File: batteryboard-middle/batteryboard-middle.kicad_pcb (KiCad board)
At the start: 2 copper layers, 46.8 x 46.8 mm, 9 parts, among them J1 FLE-107-01-G-DV-A, J2 Conn_01x02, J3 Conn_01x02, J4 FTS-107-01-L-DV-A

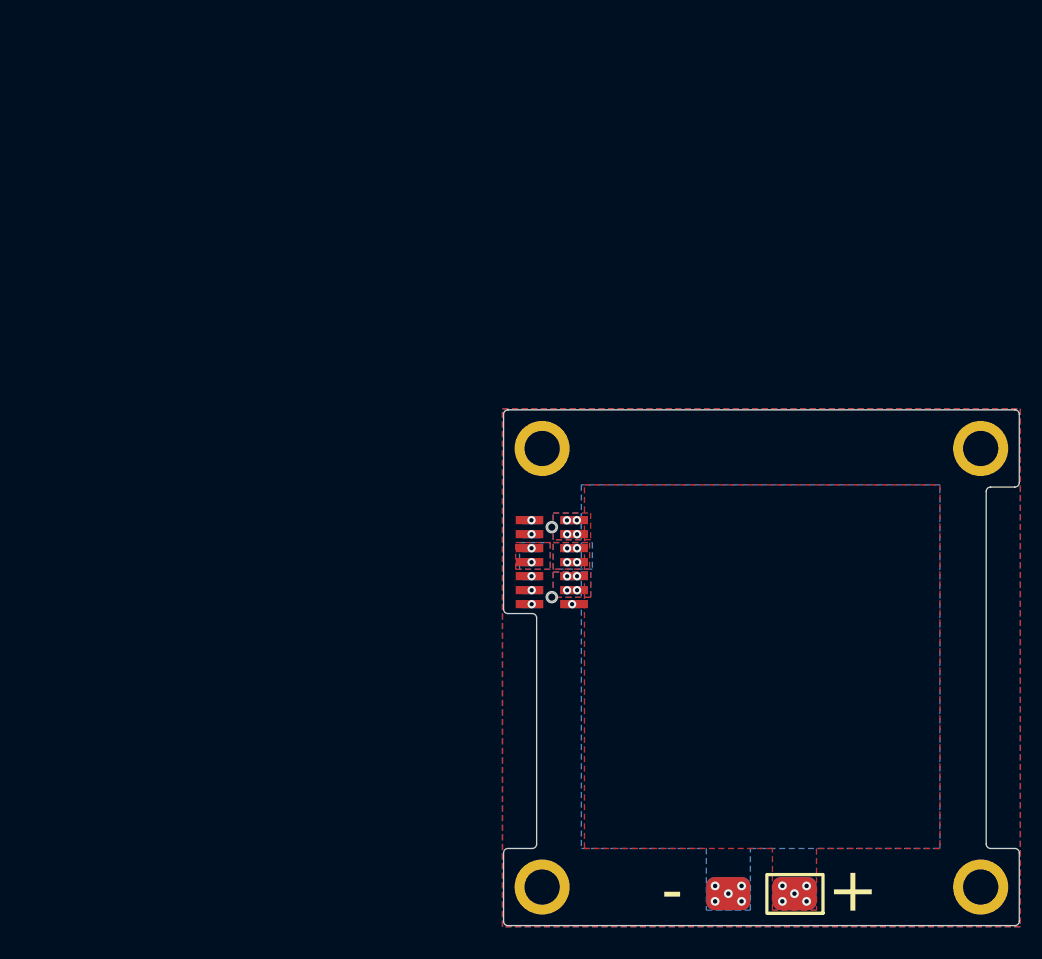
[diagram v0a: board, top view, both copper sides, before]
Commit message: Updated batteryboards for Rev B3/01
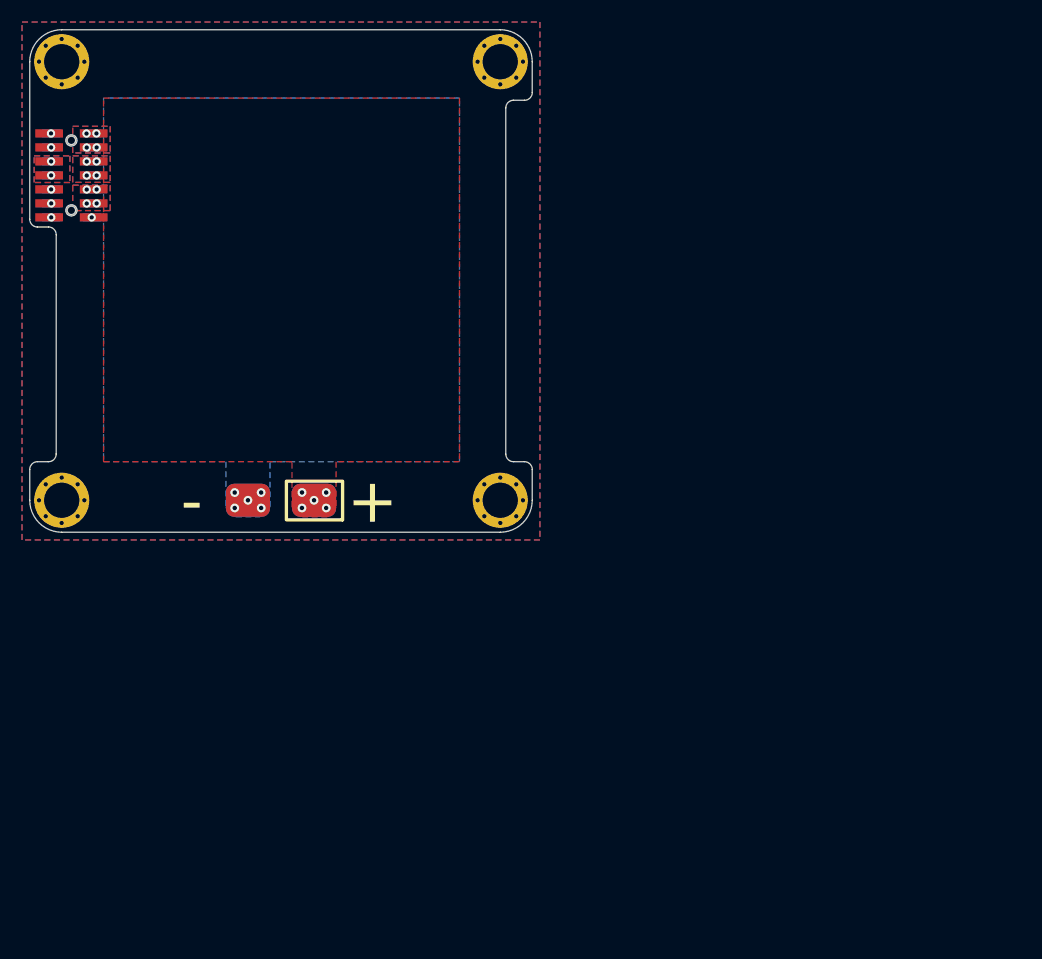
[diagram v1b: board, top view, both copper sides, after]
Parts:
- J1: value FLE-107-01-G-DV-A -> FLE-107-01-X-DV-A; footprint batteryboard:SAMTEC_FLE-107-01-G-DV-A -> batteryboard:SAMTEC_FLE-107-01-X-DV-A
- J2: renamed from J4; value FTS-107-01-L-DV-A -> FTS-107-01-X-DV-A
- J3: value Conn_01x02 -> Battery Pads
- J4: renamed from J2; value Conn_01x02 -> Battery Pads
- moved J3 56.4 mm to (103.2, 85.4)
- moved J4 56.4 mm to (103.2, 85.4)
- moved Ref** 56.2 mm to (103.0, 45.0)
- moved H4 56.0 mm to (83.3, 45.6)
- moved H1 56.0 mm to (123.1, 45.6)
- moved H3 56.0 mm to (83.3, 85.4)
- moved J1 56.0 mm to (84.2, 55.9)
- moved J2 56.0 mm to (84.2, 55.9)
- moved H2 56.0 mm to (123.1, 85.4)
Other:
- board size 46.8 x 46.8 mm -> 45.6 x 45.6 mm
- board text added: "18-FEB-23"
- board text added: "Rev B3/01"
- board text removed: "06-NOV-22"
- board text removed: "Rev B2/01"

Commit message: Exported Gerbers
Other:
- rule pad_to_mask_clearance: 0 -> 0.0508

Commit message: Rev B3/02 updates
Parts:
- added REF**: Fiducial_1mm_Mask2mm, Fiducial:Fiducial_1mm_Mask2mm, F.Cu at (119.1, 85.4)
- added REF**: Fiducial_1mm_Mask2mm, Fiducial:Fiducial_1mm_Mask2mm, F.Cu at (119.1, 45.6)
- added REF**: Fiducial_1mm_Mask2mm, Fiducial:Fiducial_1mm_Mask2mm, F.Cu at (87.3, 45.6)
- added REF**: Fiducial_1mm_Mask2mm, Fiducial:Fiducial_1mm_Mask2mm, B.Cu at (87.3, 45.6)
- added REF**: Fiducial_1mm_Mask2mm, Fiducial:Fiducial_1mm_Mask2mm, B.Cu at (119.1, 85.4)
- added REF**: Fiducial_1mm_Mask2mm, Fiducial:Fiducial_1mm_Mask2mm, B.Cu at (119.1, 45.6)
- moved Ref** 0.90 mm to (103.9, 45.0)
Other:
- board text added: "12-APR-23"
- board text added: "Rev B3/02"
- board text removed: "18-FEB-23"
- board text removed: "Rev B3/01"
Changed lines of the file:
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@@
     )
+  )
+  (footprint "Fiducial:Fiducial_1mm_Mask2mm" (layer "F.Cu")
+    (at 119.1 85.4)
+    (descr "Circular Fiducial, 1mm bare copper, 2mm soldermask opening (Level A)")
+    (tags "fiducial")
+    (attr smd)
+    (fp_text reference "REF**" (at 0 -2) (layer "F.SilkS") hide
+        (effects (font (size 1 1) (thickness 0.15)))
+    )
+    (fp_text value "Fiducial_1mm_Mask2mm" (at 0 2) (layer "F.Fab")
+        (effects (font (size 1 1) (thickness 0.15)))
+    )
+    (fp_circle (center 0 0) (end 1.25 0)
+      (stroke (width 0.05) (type solid)) (fill none) (layer "F.CrtYd"))
+    (pad "" smd circle (at 0 0) (size 1 1) (layers "F.Cu" "F.Mask")
+      (solder_mask_margin 0.5) (clearance 0.5))
   )
   (footprint "custom-footprints:pycubed_mini_half" (layer "F.Cu")
-    (at 103 45)
+    (at 103.9 45)
     (attr through_hole)
     (fp_text reference "Ref**" (at 0 0) (layer "F.SilkS") hide
@@
       (net 3 "GND") (pinfunction "1") (pintype "input"))
   )
+  (footprint "Fiducial:Fiducial_1mm_Mask2mm" (layer "F.Cu")
+    (at 119.1 45.6)
+    (descr "Circular Fiducial, 1mm bare copper, 2mm soldermask opening (Level A)")
+    (tags "fiducial")
+    (attr smd)
+    (fp_text reference "REF**" (at 0 -2) (layer "F.SilkS") hide
+        (effects (font (size 1 1) (thickness 0.15)))
+    )
+    (fp_text value "Fiducial_1mm_Mask2mm" (at 0 2) (layer "F.Fab")
+        (effects (font (size 1 1) (thickness 0.15)))
+    )
+    (fp_circle (center 0 0) (end 1.25 0)
+      (stroke (width 0.05) (type solid)) (fill none) (layer "F.CrtYd"))
+    (pad "" smd circle (at 0 0) (size 1 1) (layers "F.Cu" "F.Mask")
+      (solder_mask_margin 0.5) (clearance 0.5))
+  )
+  (footprint "Fiducial:Fiducial_1mm_Mask2mm" (layer "F.Cu")
+    (at 87.3 45.6)
+    (descr "Circular Fiducial, 1mm bare copper, 2mm soldermask opening (Level A)")
+    (tags "fiducial")
+    (attr smd)
+    (fp_text reference "REF**" (at 0 -2) (layer "F.SilkS") hide
+        (effects (font (size 1 1) (thickness 0.15)))
+    )
+    (fp_text value "Fiducial_1mm_Mask2mm" (at 0 2) (layer "F.Fab")
+        (effects (font (size 1 1) (thickness 0.15)))
+    )
+    (fp_circle (center 0 0) (end 1.25 0)
+      (stroke (width 0.05) (type solid)) (fill none) (layer "F.CrtYd"))
+    (pad "" smd circle (at 0 0) (size 1 1) (layers "F.Cu" "F.Mask")
+      (solder_mask_margin 0.5) (clearance 0.5))
+  )
   (footprint "batteryboard:Battery Pads" (layer "B.Cu")
     (at 103.2 85.4 180)
@@
     (pad "2" smd roundrect (at 3 0 180) (size 4 3) (layers "B.Cu" "B.Paste" "B.Mask") (roundrect_rratio 0.25)
       (net 2 "BATT_N_SW") (pinfunction "Pin_2") (pintype "passive"))
+  )
+  (footprint "Fiducial:Fiducial_1mm_Mask2mm" (layer "B.Cu")
+    (at 87.3 45.6 180)
+    (descr "Circular Fiducial, 1mm bare copper, 2mm soldermask opening (Level A)")
+    (tags "fiducial")
+    (attr smd)
+    (fp_text reference "REF**" (at 0 2) (layer "B.SilkS") hide
+        (effects (font (size 1 1) (thickness 0.15)) (justify mirror))
+    )
+    (fp_text value "Fiducial_1mm_Mask2mm" (at 0 -2) (layer "B.Fab")
+        (effects (font (size 1 1) (thickness 0.15)) (justify mirror))
+    )
+    (fp_circle (center 0 0) (end 1.25 0)
+      (stroke (width 0.05) (type solid)) (fill none) (layer "B.CrtYd"))
+    (pad "" smd circle (at 0 0 180) (size 1 1) (layers "B.Cu" "B.Mask")
+      (solder_mask_margin 0.5) (clearance 0.5))
   )
   (footprint "batteryboard:SAMTEC_FLE-107-01-X-DV-A" (layer "B.Cu")
@@
     )
   )
+  (footprint "Fiducial:Fiducial_1mm_Mask2mm" (layer "B.Cu")
+    (at 119.1 85.4 180)
+    (descr "Circular Fiducial, 1mm bare copper, 2mm soldermask opening (Level A)")
+    (tags "fiducial")
+    (attr smd)
+    (fp_text reference "REF**" (at 0 2) (layer "B.SilkS") hide
+        (effects (font (size 1 1) (thickness 0.15)) (justify mirror))
+    )
+    (fp_text value "Fiducial_1mm_Mask2mm" (at 0 -2) (layer "B.Fab")
+        (effects (font (size 1 1) (thickness 0.15)) (justify mirror))
+    )
+    (fp_circle (center 0 0) (end 1.25 0)
+      (stroke (width 0.05) (type solid)) (fill none) (layer "B.CrtYd"))
+    (pad "" smd circle (at 0 0 180) (size 1 1) (layers "B.Cu" "B.Mask")
+      (solder_mask_margin 0.5) (clearance 0.5))
+  )
+  (footprint "Fiducial:Fiducial_1mm_Mask2mm" (layer "B.Cu")
+    (at 119.1 45.6 180)
+    (descr "Circular Fiducial, 1mm bare copper, 2mm soldermask opening (Level A)")
+    (tags "fiducial")
+    (attr smd)
+    (fp_text reference "REF**" (at 0 2) (layer "B.SilkS") hide
+        (effects (font (size 1 1) (thickness 0.15)) (justify mirror))
+    )
+    (fp_text value "Fiducial_1mm_Mask2mm" (at 0 -2) (layer "B.Fab")
+        (effects (font (size 1 1) (thickness 0.15)) (justify mirror))
+    )
+    (fp_circle (center 0 0) (end 1.25 0)
+      (stroke (width 0.05) (type solid)) (fill none) (layer "B.CrtYd"))
+    (pad "" smd circle (at 0 0 180) (size 1 1) (layers "B.Cu" "B.Mask")
+      (solder_mask_margin 0.5) (clearance 0.5))
+  )
+  (gr_line (start 103.2 88.3) (end 103.2 42.7)
+    (stroke (width 0.15) (type default)) (layer "Dwgs.User"))
+  (gr_line (start 123.1 45.6) (end 83.3 45.6)
+    (stroke (width 0.15) (type default)) (layer "Dwgs.User"))
   (gr_arc (start 82.1 60.6) (mid 82.594975 60.805025) (end 82.8 61.3)
     (stroke (width 0.0254) (type default)) (layer "Edge.Cuts"))
@@
     (effects (font (size 4 4) (thickness 0.7)) (justify mirror))
   )
-  (gr_text "18-FEB-23" (at 104 44.7) (layer "F.Mask")
+  (gr_text "12-APR-23" (at 104.9 44.7) (layer "F.Mask")
     (effects (font (size 0.635 0.635) (thickness 0.1524)) (justify right))
   )
-  (gr_text "Rev B3/01" (at 106.0168 47.2) (layer "F.Mask")
+  (gr_text "Rev B3/02" (at 106.9 47.1) (layer "F.Mask")
     (effects (font (size 0.635 0.635) (thickness 0.1524)) (justify right))
   )

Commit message: Updated BOMs and STEP files
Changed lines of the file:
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@@
     (property "Sheetfile" "batteryboard-middle.kicad_sch")
     (property "Sheetname" "")
+    (property "exclude_from_bom" "")
     (property "ki_description" "Mounting Hole with connection")
     (property "ki_keywords" "mounting hole")
@@
     (property "Sheetfile" "batteryboard-middle.kicad_sch")
     (property "Sheetname" "")
+    (property "exclude_from_bom" "")
     (property "ki_description" "Mounting Hole with connection")
     (property "ki_keywords" "mounting hole")
@@
     (property "Sheetfile" "batteryboard-middle.kicad_sch")
     (property "Sheetname" "")
+    (property "exclude_from_bom" "")
     (property "ki_description" "Generic connector, single row, 01x02, script generated (kicad-library-utils/schlib/autogen/connector/)")
     (property "ki_keywords" "connector")
-    (attr smd)
+    (attr smd exclude_from_bom)
     (fp_text reference "J3" (at -7.111997 -0.000005 180 unlocked) (layer "F.SilkS") hide
         (effects (font (size 1 1) (thickness 0.15)))
@@
     (descr "Circular Fiducial, 1mm bare copper, 2mm soldermask opening (Level A)")
     (tags "fiducial")
-    (attr smd)
+    (attr smd exclude_from_bom)
     (fp_text reference "REF**" (at 0 -2) (layer "F.SilkS") hide
         (effects (font (size 1 1) (thickness 0.15)))
@@
   (footprint "custom-footprints:pycubed_mini_half" (layer "F.Cu")
     (at 103.9 45)
-    (attr through_hole)
+    (attr through_hole exclude_from_bom)
     (fp_text reference "Ref**" (at 0 0) (layer "F.SilkS") hide
         (effects (font (size 1.27 1.27) (thickness 0.15)))
@@
     (property "Sheetfile" "batteryboard-middle.kicad_sch")
     (property "Sheetname" "")
+    (property "exclude_from_bom" "")
     (property "ki_description" "Mounting Hole with connection")
     (property "ki_keywords" "mounting hole")
@@
     (property "Sheetfile" "batteryboard-middle.kicad_sch")
     (property "Sheetname" "")
+    (property "exclude_from_bom" "")
     (property "ki_description" "Mounting Hole with connection")
     (property "ki_keywords" "mounting hole")
@@
     (descr "Circular Fiducial, 1mm bare copper, 2mm soldermask opening (Level A)")
     (tags "fiducial")
-    (attr smd)
+    (attr smd exclude_from_bom)
     (fp_text reference "REF**" (at 0 -2) (layer "F.SilkS") hide
         (effects (font (size 1 1) (thickness 0.15)))
@@
     (descr "Circular Fiducial, 1mm bare copper, 2mm soldermask opening (Level A)")
     (tags "fiducial")
-    (attr smd)
+    (attr smd exclude_from_bom)
     (fp_text reference "REF**" (at 0 -2) (layer "F.SilkS") hide
         (effects (font (size 1 1) (thickness 0.15)))
@@
     (property "Sheetfile" "batteryboard-middle.kicad_sch")
     (property "Sheetname" "")
+    (property "exclude_from_bom" "")
     (property "ki_description" "Generic connector, single row, 01x02, script generated (kicad-library-utils/schlib/autogen/connector/)")
     (property "ki_keywords" "connector")
-    (attr smd)
+    (attr smd exclude_from_bom)
     (fp_text reference "J4" (at -7.112 0 180 unlocked) (layer "B.SilkS") hide
         (effects (font (size 1 1) (thickness 0.15)) (justify mirror))
@@
     (descr "Circular Fiducial, 1mm bare copper, 2mm soldermask opening (Level A)")
     (tags "fiducial")
-    (attr smd)
+    (attr smd exclude_from_bom)
     (fp_text reference "REF**" (at 0 2) (layer "B.SilkS") hide
         (effects (font (size 1 1) (thickness 0.15)) (justify mirror))
@@
     (descr "Circular Fiducial, 1mm bare copper, 2mm soldermask opening (Level A)")
     (tags "fiducial")
-    (attr smd)
+    (attr smd exclude_from_bom)
     (fp_text reference "REF**" (at 0 2) (layer "B.SilkS") hide
         (effects (font (size 1 1) (thickness 0.15)) (justify mirror))
@@
     (descr "Circular Fiducial, 1mm bare copper, 2mm soldermask opening (Level A)")
     (tags "fiducial")
-    (attr smd)
+    (attr smd exclude_from_bom)
     (fp_text reference "REF**" (at 0 2) (layer "B.SilkS") hide
         (effects (font (size 1 1) (thickness 0.15)) (justify mirror))
@@
   (gr_line (start 123.1 88.3) (end 83.3 88.3)
     (stroke (width 0.0254) (type solid)) (layer "Edge.Cuts"))
-  (gr_text "+" (at 111.5 85.5) (layer "B.SilkS")
+  (gr_text "+" (at 111.5 85.1) (layer "B.SilkS")
     (effects (font (size 4 4) (thickness 0.7)) (justify mirror))
   )
-  (gr_text "-" (at 95.1 85.5) (layer "B.SilkS")
+  (gr_text "-" (at 95.1 85.1) (layer "B.SilkS")
     (effects (font (size 4 4) (thickness 0.7)) (justify mirror))
   )
-  (gr_text "+" (at 111.5 85.5) (layer "F.SilkS")
+  (gr_text "+" (at 111.5 85.1) (layer "F.SilkS")
     (effects (font (size 4 4) (thickness 0.7)) (justify mirror))
   )
-  (gr_text "-" (at 95.1 85.5) (layer "F.SilkS")
+  (gr_text "-" (at 95.1 85.1) (layer "F.SilkS")
     (effects (font (size 4 4) (thickness 0.7)) (justify mirror))
   )
@@
     (effects (font (size 0.635 0.635) (thickness 0.1524)) (justify right))
   )
+  (dimension (type aligned) (layer "Dwgs.User")
+    (pts (xy 80.4 45.6) (xy 126 45.600006))
+    (height -6.729953)
+    (gr_text "1795.2756 mils" (at 103.200001 37.72005 359.9999925) (layer "Dwgs.User")
+      (effects (font (size 1 1) (thickness 0.15)))
+    )
+    (format (prefix "") (suffix "") (units 3) (units_format 1) (precision 4))
+    (style (thickness 0.15) (arrow_length 1.27) (text_position_mode 0) (extension_height 0.58642) (extension_offset 0.5) keep_text_aligned)
+  )
+  (dimension (type aligned) (layer "Dwgs.User")
+    (pts (xy 83.3 42.7) (xy 83.3 88.3))
+    (height 6.9)
+    (gr_text "1795.2756 mils" (at 75.25 65.5 90) (layer "Dwgs.User")
+      (effects (font (size 1 1) (thickness 0.15)))
+    )
+    (format (prefix "") (suffix "") (units 3) (units_format 1) (precision 4))
+    (style (thickness 0.15) (arrow_length 1.27) (text_position_mode 0) (extension_height 0.58642) (extension_offset 0.5) keep_text_aligned)
+  )
   (via (at 86.47 55.92) (size 0.762) (drill 0.381) (layers "F.Cu" "B.Cu") (net 1))
